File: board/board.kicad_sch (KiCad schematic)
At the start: 1 part, among them U1 ESP32-DevKitC

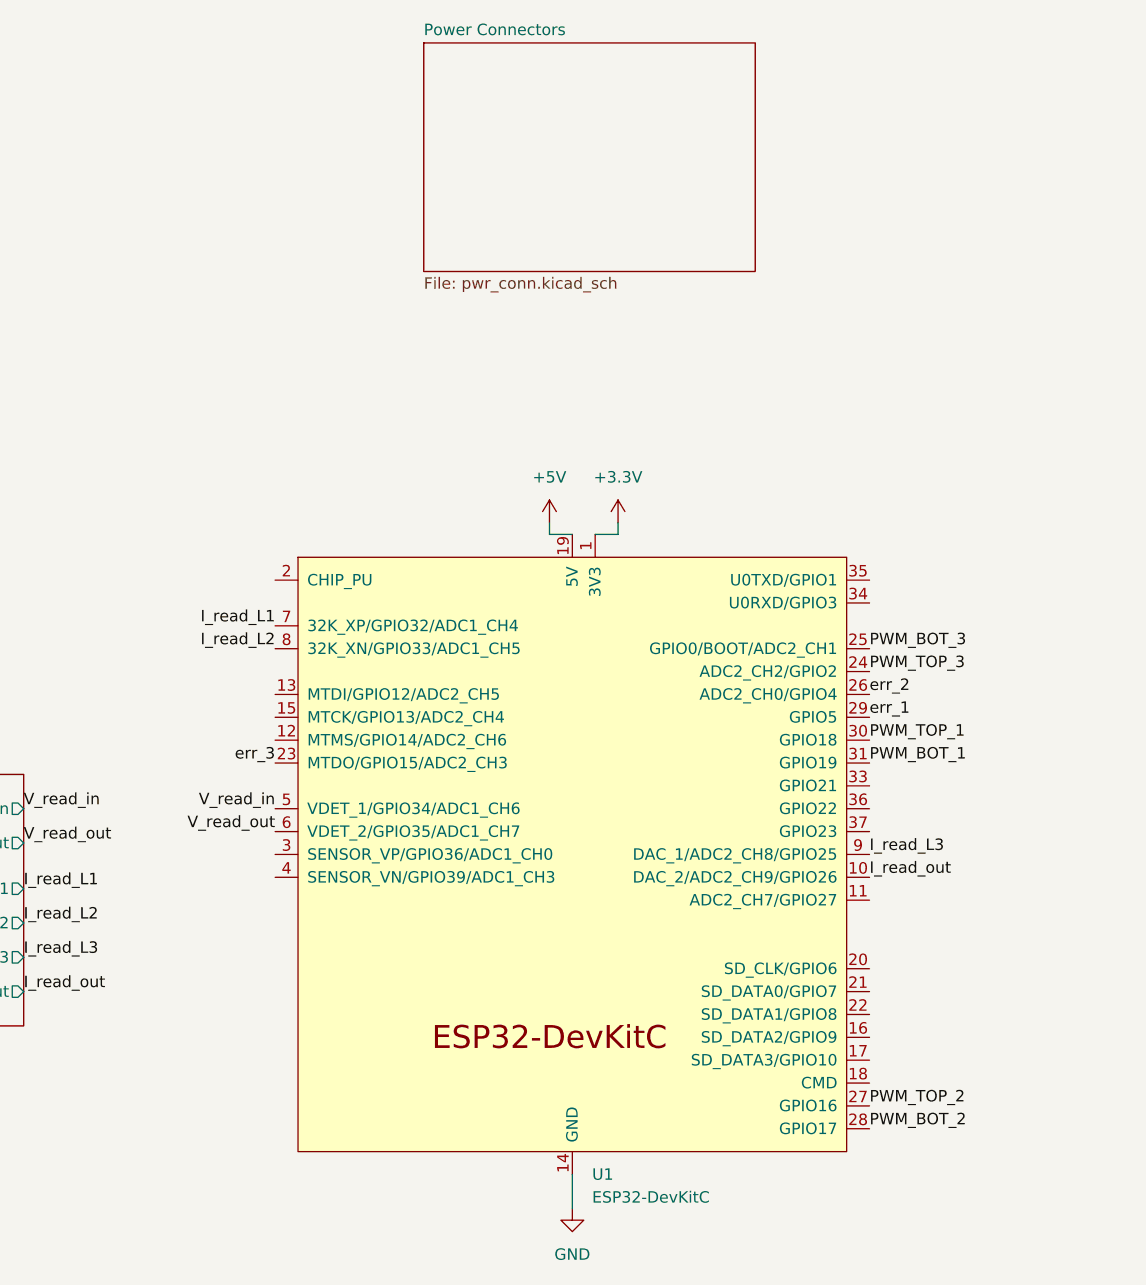
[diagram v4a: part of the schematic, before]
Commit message: Finalização da placa, trilhas, planos de terra e footprint TJA1050
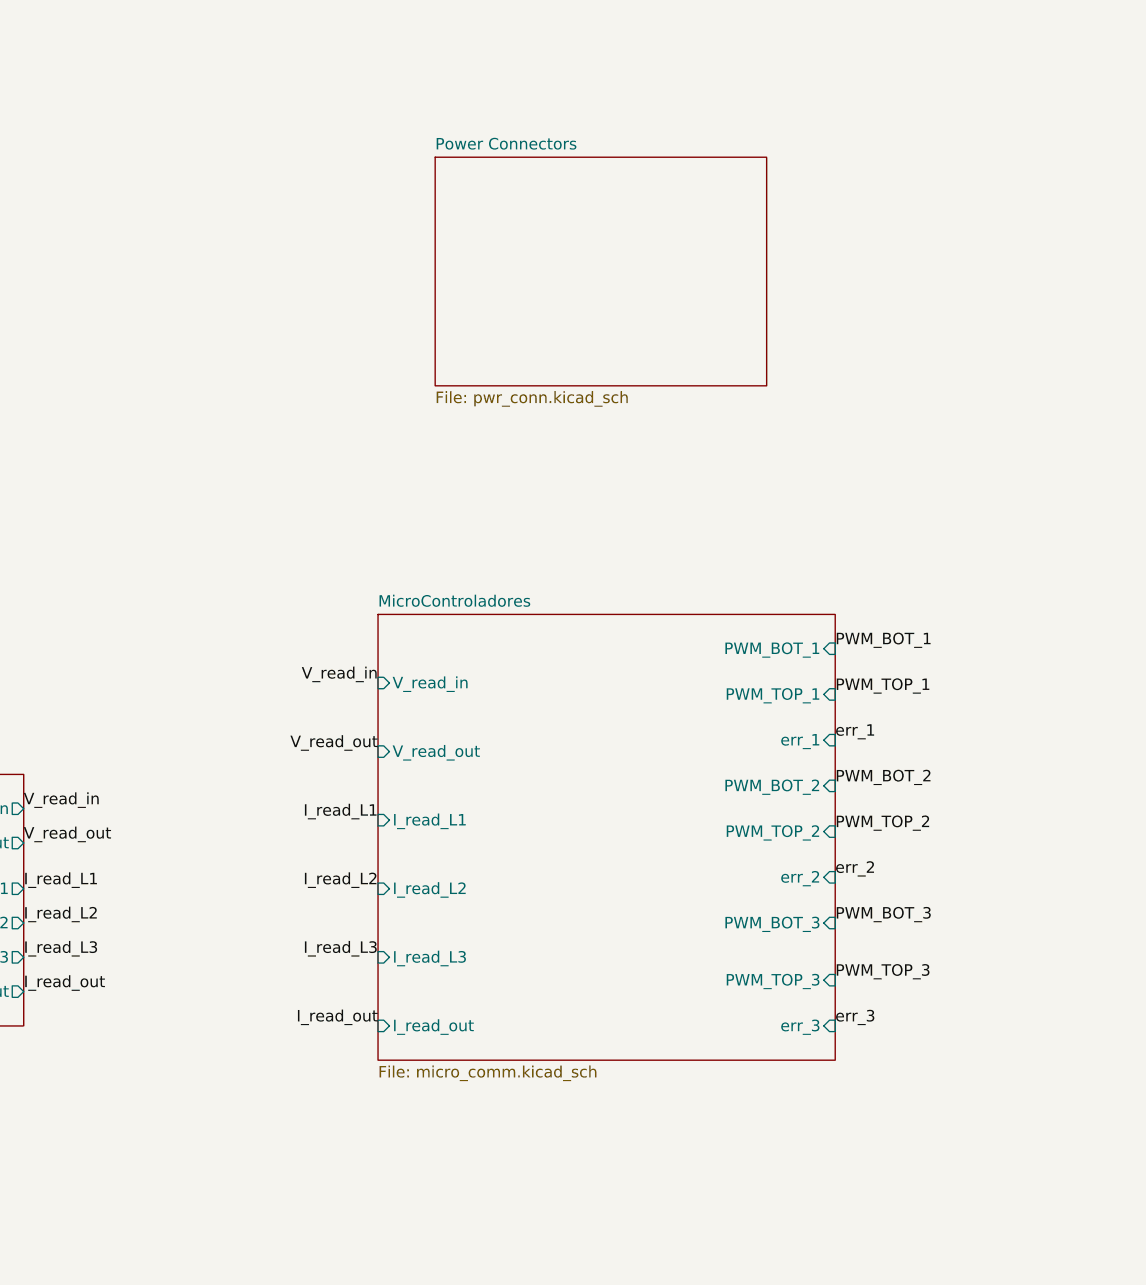
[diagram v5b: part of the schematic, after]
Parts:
- removed U1: ESP32-DevKitC, PCM_Espressif:ESP32-DevKitC, symbol PCM_Espressif:ESP32-DevKitC
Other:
- added sheet MicroControladores (micro_comm.kicad_sch)

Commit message: Criação da placa de alimentação
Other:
- company: (none) -> Escola Politécnica da Universidade de São Paulo
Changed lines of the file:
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@@
 	(generator_version "8.0")
 	(paper "A4")
+	(title_block
+		(date "2025-10-02")
+		(rev "01")
+		(company "Escola Politécnica da Universidade de São Paulo")
+	)
 	(label "err_1"
 		(at 177.8 96.52 0)
@@
 			(project "board"
 				(path "/d7be55ed-3561-4de6-aa99-76e883d44fb9"
-					(page "9")
+					(page "7")
 				)
 			)
@@
 			(project "board"
 				(path "/d7be55ed-3561-4de6-aa99-76e883d44fb9"
-					(page "29")
+					(page "20")
 				)
 			)
@@
 			(project "board"
 				(path "/d7be55ed-3561-4de6-aa99-76e883d44fb9"
-					(page "9")
-				)
-			)
+					(page "2")
+				)
+			)
